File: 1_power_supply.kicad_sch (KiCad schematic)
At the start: 40 parts, among them J2 Conn_01x03_Pin, U101 TPS54332D, U102 TPS561208D, U103 TLV75533PDBV

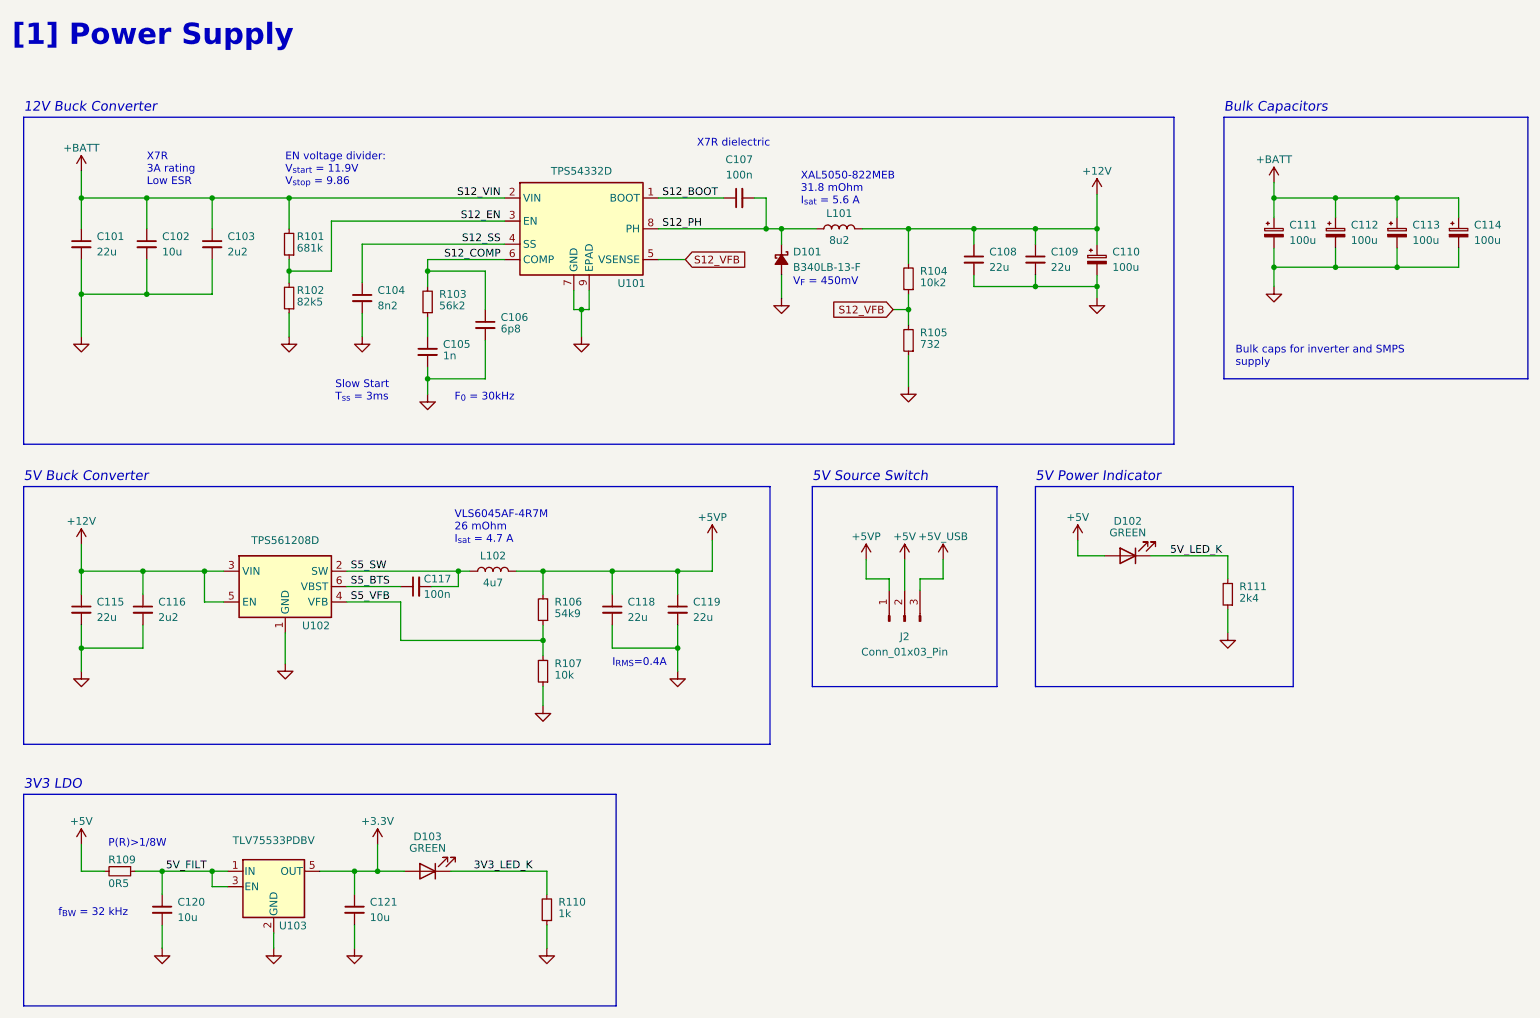
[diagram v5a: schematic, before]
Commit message: feat: LED routing, encoder interface, footprint updates
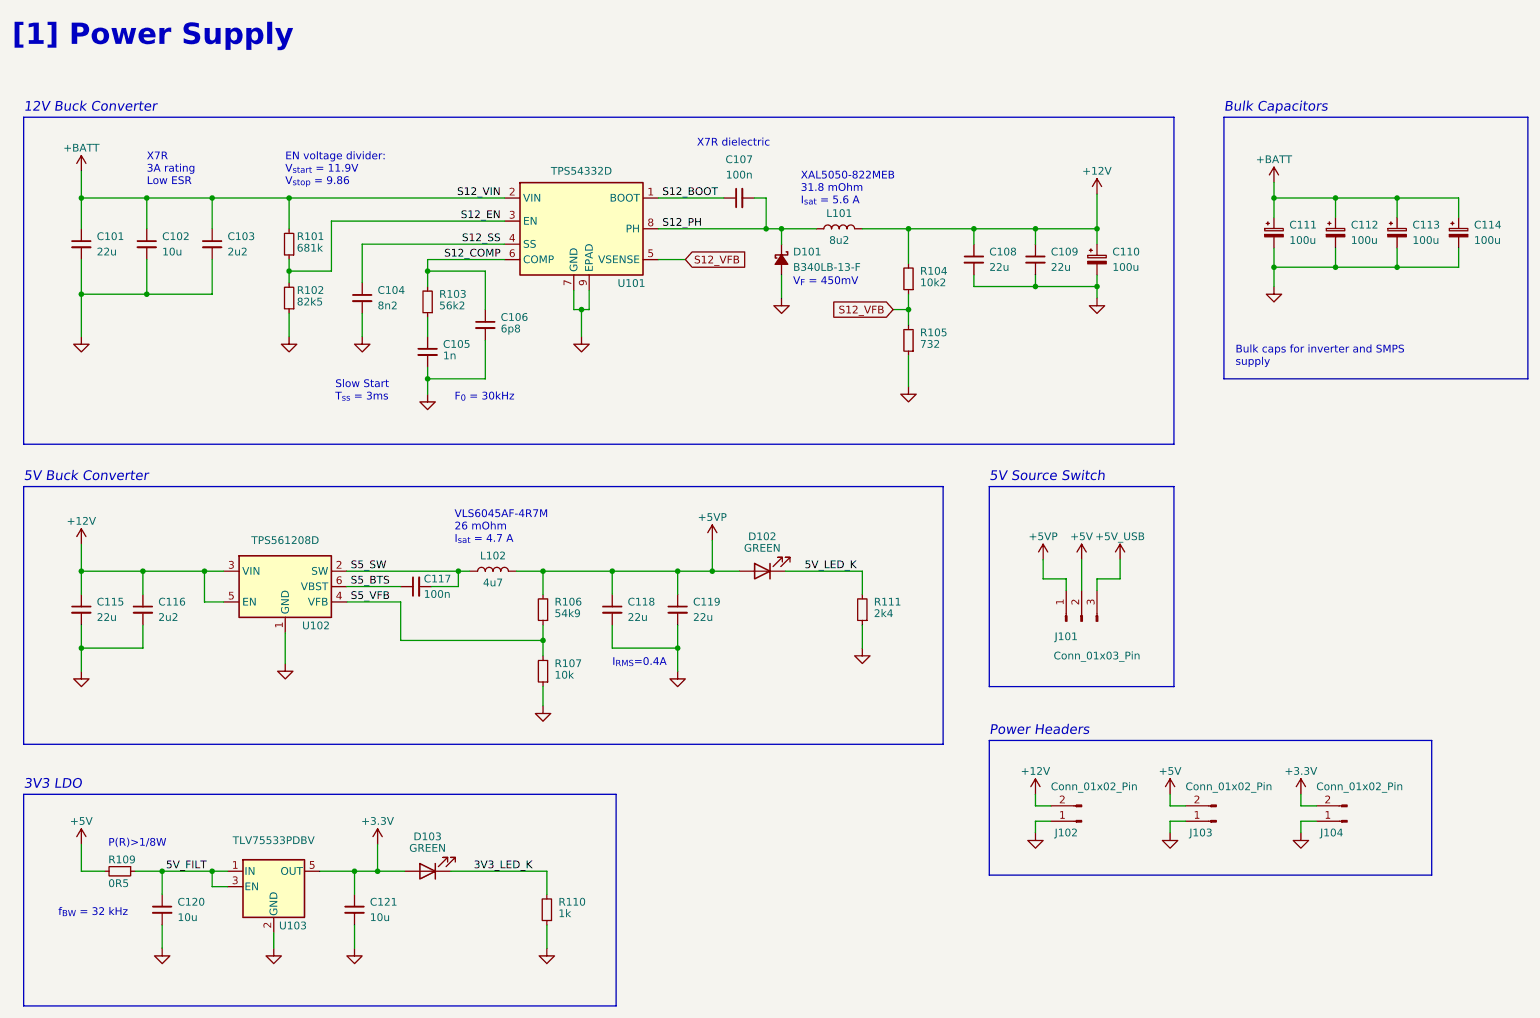
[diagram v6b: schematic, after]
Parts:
- added J102, J103, J104: Conn_01x02_Pin, symbol Connector:Conn_01x02_Pin
- C101, C108, C109, C115, C118, C119: footprint (none) -> Capacitor_SMD:C_0603_1608Metric_Pad1.08x0.95mm_HandSolder
- renumbered J2 to J101
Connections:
- net +12V: now also J102.2 (Pin_2)
- net +3.3V: now also J104.2 (Pin_2)
- net +5V: now also J103.2 (Pin_2); no longer D102.2 (A)
- net +5VP: now also D102.2 (A)
- net GND: now also J102.1 (Pin_1), J103.1 (Pin_1), J104.1 (Pin_1)
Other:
- note added: "Power Headers"
- note removed: "5V Power Indicator"
- title: Power Supply [1] -> Power Supply
- moved on the sheet: D102, J101, R111

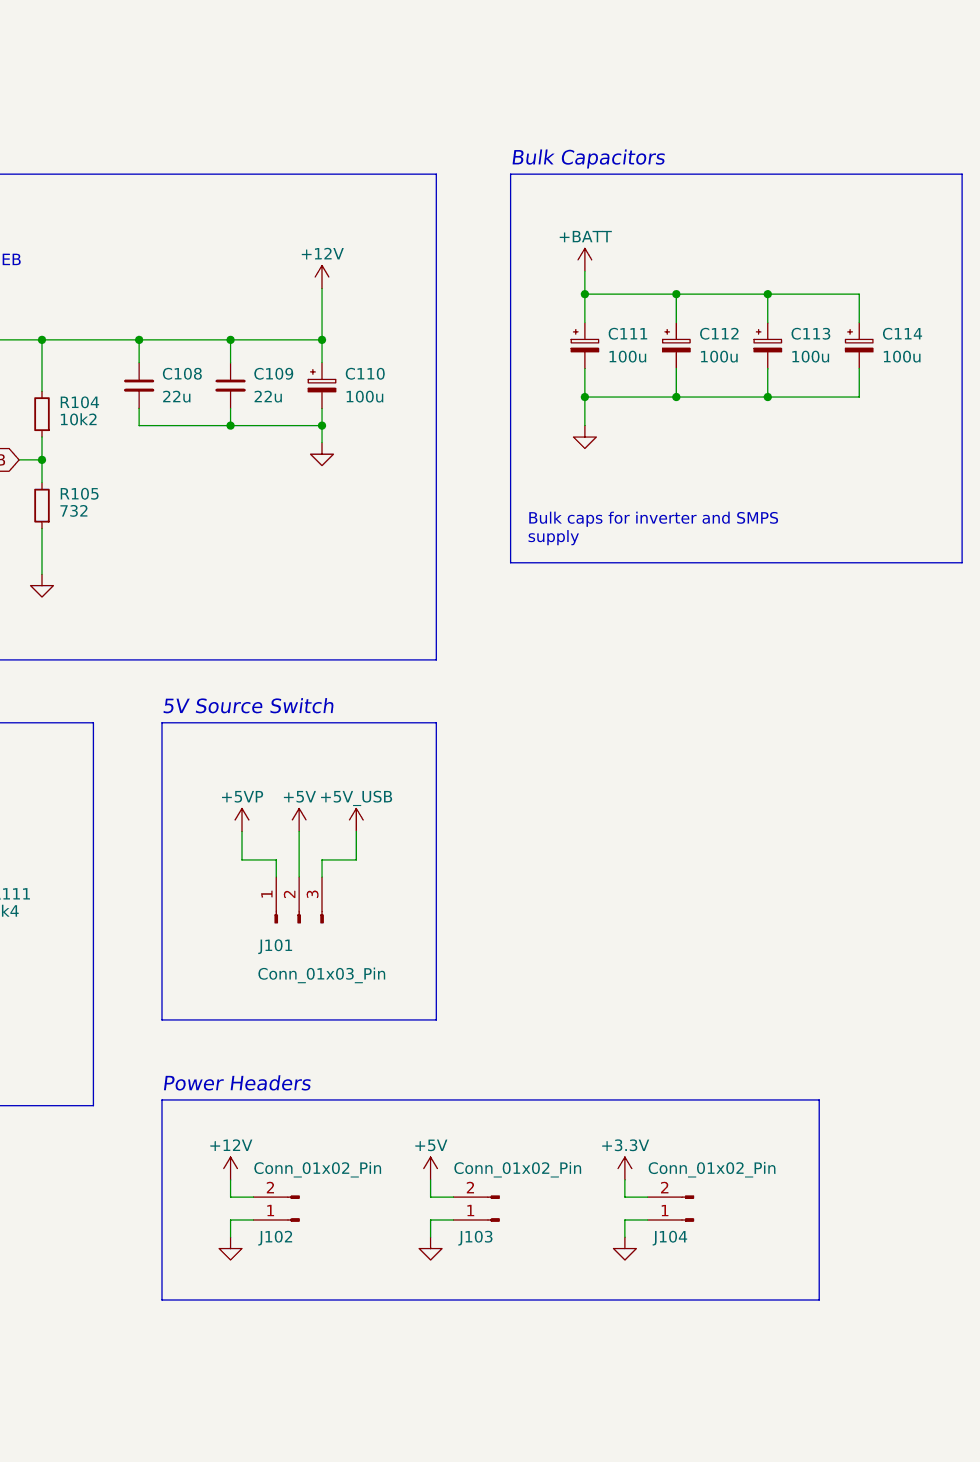
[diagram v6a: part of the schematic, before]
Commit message: feat: footprint assignment, circuit check and routing kickoff
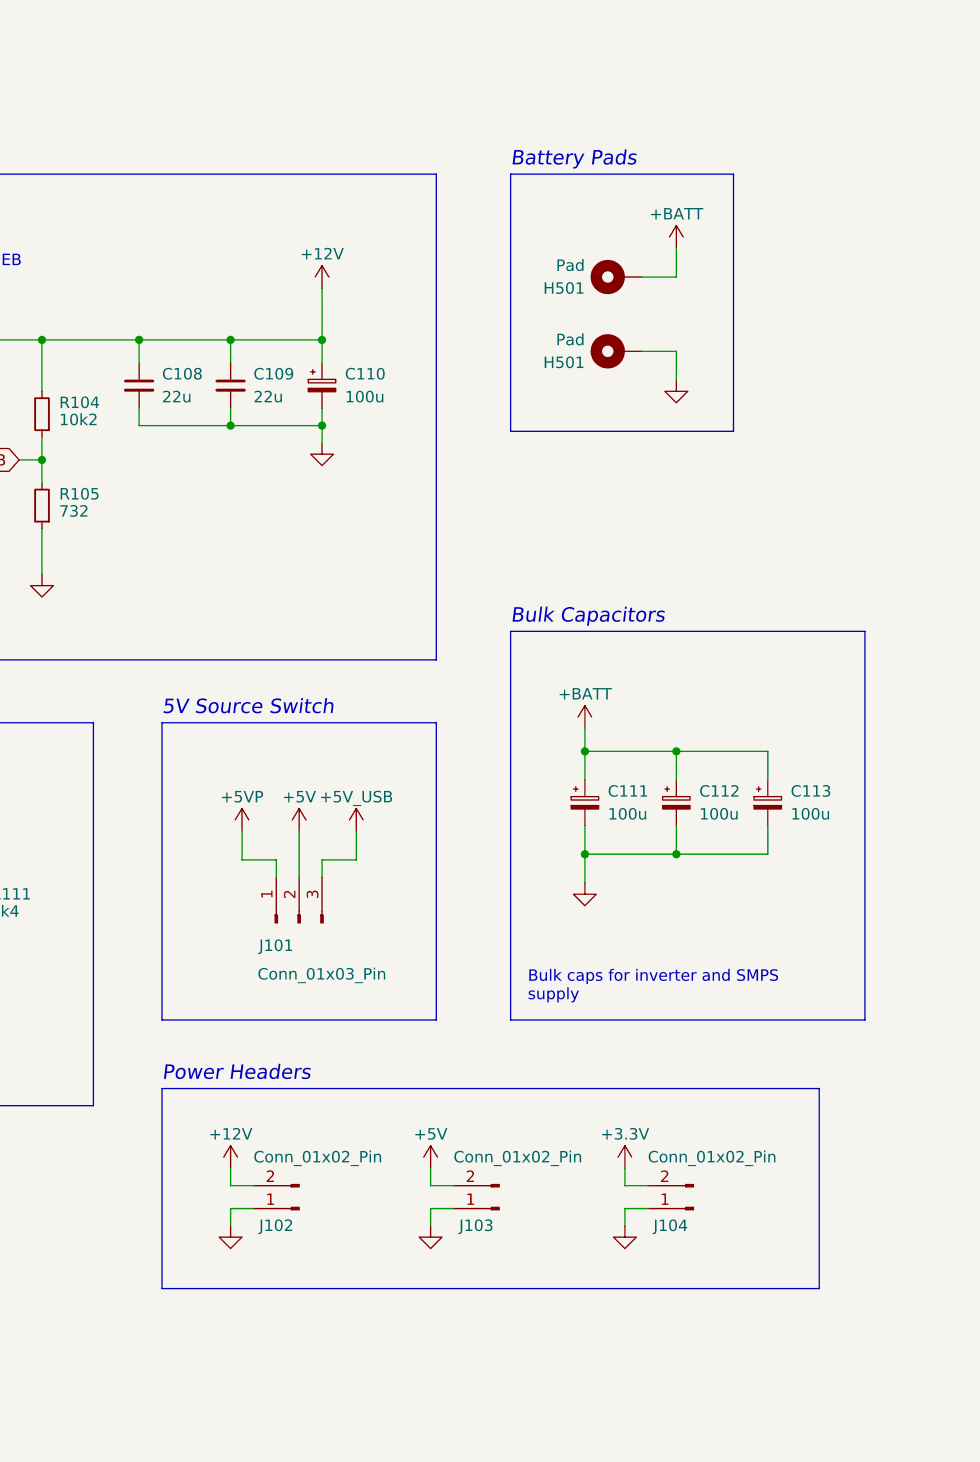
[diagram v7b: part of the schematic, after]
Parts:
- removed C114: 100u, symbol Device:C_Polarized_Small
- added H501 (x2): Pad, TestPoint:TestPoint_THTPad_4.0x4.0mm_Drill2.0mm, symbol Mechanical:MountingHole_Pad
- C102, C103, C116, C120, C121: footprint (none) -> Capacitor_SMD:C_0603_1608Metric_Pad1.08x0.95mm_HandSolder
- C104, C105, C106, C107, C117: footprint (none) -> Capacitor_SMD:C_0402_1005Metric_Pad0.74x0.62mm_HandSolder
- C110, C111, C112, C113: footprint (none) -> Capacitor_SMD:CP_Elec_6.3x7.7; Link (none) -> https://www.digikey.de/en/products/detail/panasonic-electro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
- D101: Link (none) -> https://www.digikey.de/en/products/detail/diodes-incorporat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
- D102, D103: footprint (none) -> LED_SMD:LED_0603_1608Metric_Pad1.05x0.95mm_HandSolder; Link (none) -> https://www.digikey.de/en/products/detail/liteon/LTST-C190K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
- J101: footprint (none) -> Connector_PinHeader_2.54mm:PinHeader_1x03_P2.54mm_Vertical
- J102, J103, J104: footprint (none) -> Connector_PinHeader_2.54mm:PinHeader_1x02_P2.54mm_Vertical
- L101: footprint (none) -> Inductor_SMD:L_Coilcraft_XAL5050-XXX; Link (none) -> https://www.mouser.de/ProductDetail/Coilcraft/XAL5050-822ME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
- L102: footprint Inductor_TDK:VLS6045 -> Inductor_SMD:L_TDK_VLS6045EX_VLS6045AF; Link (none) -> https://www.digikey.de/en/products/detail/tdk-corporation/V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
- R101, R102, R104, R105, R106, R107, R109, R110, R111: footprint (none) -> Resistor_SMD:R_0603_1608Metric_Pad0.98x0.95mm_HandSolder
- R103: footprint (none) -> Resistor_SMD:R_0402_1005Metric_Pad0.72x0.64mm_HandSolder
- U101: footprint (none) -> Package_SO:TI_SO-PowerPAD-8; Link (none) -> https://www.digikey.de/en/products/detail/texas-instruments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
- U102: footprint (none) -> Package_TO_SOT_SMD:SOT-23-6; Link (none) -> https://www.digikey.de/en/products/detail/texas-instruments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
- U103: Link (none) -> https://www.digikey.de/en/products/detail/texas-instruments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
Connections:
- net +BATT: now also H501.1
- net GND: now also H501.1
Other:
- note added: "Battery Pads"
- moved on the sheet: C111, C112, C113, J102, J103, J104

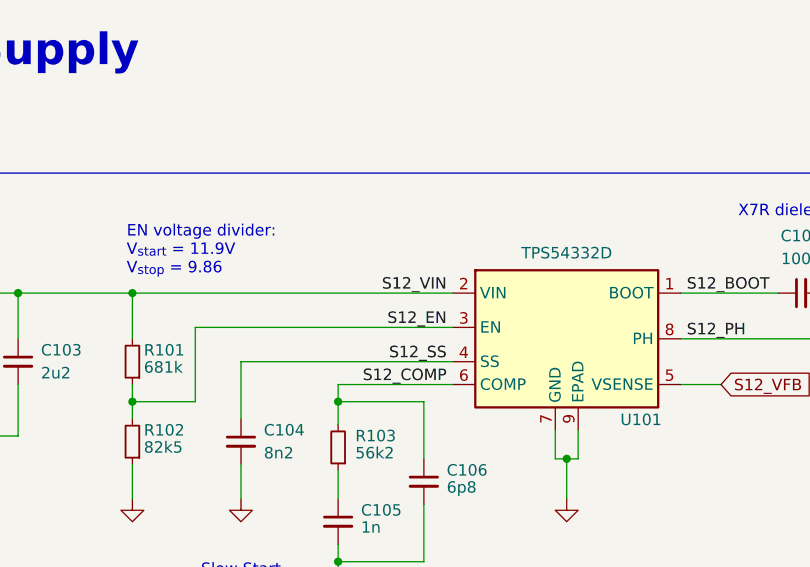
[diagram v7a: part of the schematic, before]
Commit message: feat: single phase, HSE, CAN routing and general layout
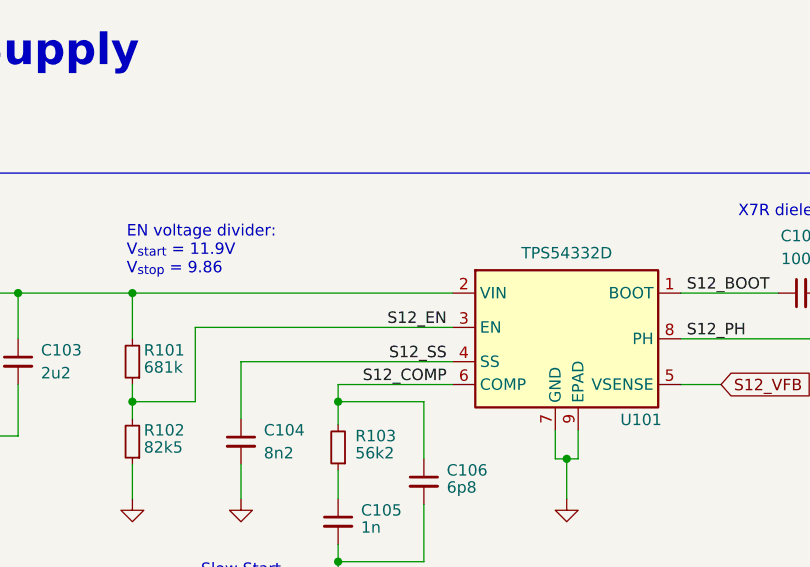
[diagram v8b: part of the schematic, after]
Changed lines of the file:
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@@
     (effects (font (size 1.27 1.27)) (justify left bottom))
-  )
-  (label "S12_VIN" (at 99.06 50.165 180) (fields_autoplaced)
-    (effects (font (size 1.27 1.27)) (justify right bottom))
   )
   (label "S12_COMP" (at 99.06 60.325 180) (fields_autoplaced)
@@
     )
   )
-  (symbol (lib_id "power:+3.3V") (at 78.74 156.845 0) (unit 1)
+  (symbol (lib_name "+3.3V_1") (lib_id "power:+3.3V") (at 78.74 156.845 0) (unit 1)
     (in_bom yes) (on_board yes) (dnp no)
     (property "Reference" "#PWR0103" (at 78.74 160.655 0)
@@
     )
   )
-  (symbol (lib_id "power:+5V") (at 29.845 156.845 0) (unit 1)
+  (symbol (lib_name "+5V_1") (lib_id "power:+5V") (at 29.845 156.845 0) (unit 1)
     (in_bom yes) (on_board yes) (dnp no)
     (property "Reference" "#PWR0104" (at 29.845 160.655 0)
@@
     )
   )
-  (symbol (lib_id "power:+BATT") (at 236.855 45.085 0) (unit 1)
+  (symbol (lib_name "+BATT_1") (lib_id "power:+BATT") (at 236.855 45.085 0) (unit 1)
     (in_bom yes) (on_board yes) (dnp no)
     (property "Reference" "#PWR0201" (at 236.855 48.895 0)
@@
       (effects (font (size 1.27 1.27)))
     )
-    (property "Footprint" "Package_SO:TI_SO-PowerPAD-8" (at 112.395 55.245 0)
+    (property "Footprint" "Package_SO:TI_SO-PowerPAD-8" (at 112.395 76.835 0)
       (effects (font (size 1.27 1.27)) hide)
     )
@@
       (effects (font (size 1.27 1.27)) hide)
     )
-    (property "Link" "https://www.digikey.de/en/products/detail/texas-instruments/TPS54332DDAR/2232814" (at 112.395 55.245 0)
+    (property "Link" "https://www.digikey.de/en/products/detail/texas-instruments/TPS54332DDAR/2232814" (at 112.395 76.835 0)
       (effects (font (size 1.27 1.27)) hide)
     )
@@
     )
   )
-  (symbol (lib_id "power:+12V") (at 29.845 107.315 0) (unit 1)
+  (symbol (lib_name "+12V_1") (lib_id "power:+12V") (at 29.845 107.315 0) (unit 1)
     (in_bom yes) (on_board yes) (dnp no)
     (property "Reference" "#PWR0107" (at 29.845 111.125 0)
@@
     )
   )
-  (symbol (lib_id "power:+12V") (at 197.485 49.53 0) (unit 1)
+  (symbol (lib_name "+12V_2") (lib_id "power:+12V") (at 197.485 49.53 0) (unit 1)
     (in_bom yes) (on_board yes) (dnp no)
     (property "Reference" "#PWR0115" (at 197.485 53.34 0)
@@
     )
   )
-  (symbol (lib_id "power:+5V") (at 194.945 109.855 0) (unit 1)
+  (symbol (lib_name "+5V_2") (lib_id "power:+5V") (at 194.945 109.855 0) (unit 1)
     (in_bom yes) (on_board yes) (dnp no)
     (property "Reference" "#PWR06" (at 194.945 113.665 0)
@@
     )
   )
-  (symbol (lib_id "power:+BATT") (at 29.845 45.72 0) (unit 1)
+  (symbol (lib_name "+BATT_2") (lib_id "power:+BATT") (at 29.845 45.72 0) (unit 1)
     (in_bom yes) (on_board yes) (dnp no)
     (property "Reference" "#PWR0113" (at 29.845 49.53 0)
